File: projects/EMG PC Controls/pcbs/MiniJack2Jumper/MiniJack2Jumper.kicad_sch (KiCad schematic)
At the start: 1 part, among them J1 35RASMT2BHNTRX

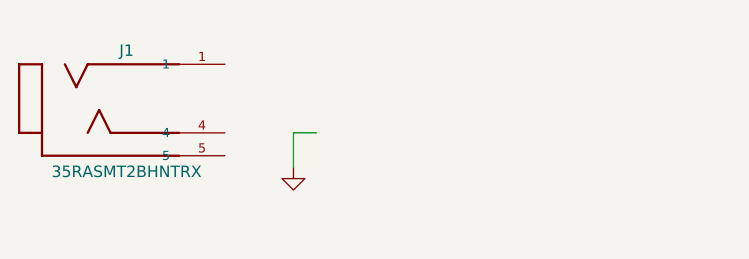
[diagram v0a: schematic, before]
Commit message: added header + BOM
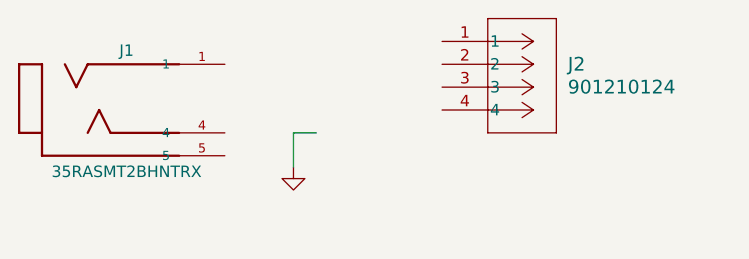
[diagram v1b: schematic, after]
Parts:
- added J2: 901210124, MiniJack2Jumper:CONN04_901210124_MOL, symbol MiniJack2Jumper:901210124
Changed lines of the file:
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@@
+	)
+	(symbol
+		(lib_id "MiniJack2Jumper:901210124")
+		(at 161.29 80.01 0)
+		(unit 1)
+		(exclude_from_sim no)
+		(in_bom yes)
+		(on_board yes)
+		(dnp no)
+		(fields_autoplaced yes)
+		(property "Reference" "J2"
+			(at 175.26 82.5499 0)
+			(effects
+				(font
+					(size 1.524 1.524)
+				)
+				(justify left)
+			)
+		)
+		(property "Value" "901210124"
+			(at 175.26 85.0899 0)
+			(effects
+				(font
+					(size 1.524 1.524)
+				)
+				(justify left)
+			)
+		)
+		(property "Footprint" "MiniJack2Jumper:CONN04_901210124_MOL"
+			(at 161.29 80.01 0)
+			(effects
+				(font
+					(size 1.27 1.27)
+					(italic yes)
+				)
+				(hide yes)
+			)
+		)
+		(property "Datasheet" "https://www.molex.com/pdm_docs/sd/901210124_sd.pdf"
+			(at 161.29 80.01 0)
+			(effects
+				(font
+					(size 1.27 1.27)
+					(italic yes)
+				)
+				(hide yes)
+			)
+		)
+		(property "Description" ""
+			(at 161.29 80.01 0)
+			(effects
+				(font
+					(size 1.27 1.27)
+				)
+				(hide yes)
+			)
+		)
+		(property "DigiKey Part Number" "23-0901210124-ND"
+			(at 161.29 80.01 0)
+			(effects
+				(font
+					(size 1.27 1.27)
+				)
+				(hide yes)
+			)
+		)
+		(property "DigiKey Link" "https://www.digikey.at/en/products/detail/molex/0901210124/760813 "
+			(at 161.29 80.01 0)
+			(effects
+				(font
+					(size 1.27 1.27)
+				)
+				(hide yes)
+			)
+		)
+		(pin "4"
+		)
+		(pin "1"
+		)
+		(pin "3"
+		)
+		(pin "2"
+		)
+		(instances
+			(project ""
+				(path "/b427ac6b-1d01-4d64-b1e2-d6e01953f973"
+					(reference "J2")
+					(unit 1)
+				)
+			)
+		)
 	)
 	(symbol

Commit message: finiished mini jack to 1x4 jumper pcb
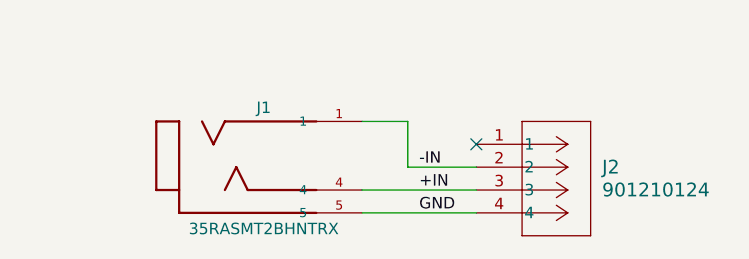
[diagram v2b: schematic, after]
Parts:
- J1: DigiKey Link (none) -> https://www.digikey.at/en/products/detail/switchcraft-inc/3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; DigiKey Part Number (none) -> SC1489-1-ND
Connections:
- net GND: now also J1.5, J2.4
- net -IN: now reaches J1.1
- net -IN: now also J2.2
- net +IN: now reaches J1.4
- net +IN: now also J2.3
- no-connect marks 0 -> 1
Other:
- moved on the sheet: J1, J2
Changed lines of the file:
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@@
 	(generator_version "8.0")
 	(paper "A4")
-	(wire
-		(pts
-			(xy 144.78 93.98) (xy 144.78 90.17)
-		)
-		(stroke
-			(width 0)
-			(type default)
-		)
-	)
-	(wire
-		(pts
-			(xy 144.78 90.17) (xy 147.32 90.17)
-		)
-		(stroke
-			(width 0)
-			(type default)
+	(no_connect
+		(at 165.1 91.44)
+	)
+	(wire
+		(pts
+			(xy 152.4 88.9) (xy 157.48 88.9)
+		)
+		(stroke
+			(width 0)
+			(type default)
+		)
+	)
+	(wire
+		(pts
+			(xy 152.4 96.52) (xy 165.1 96.52)
+		)
+		(stroke
+			(width 0)
+			(type default)
+		)
+	)
+	(wire
+		(pts
+			(xy 157.48 93.98) (xy 165.1 93.98)
+		)
+		(stroke
+			(width 0)
+			(type default)
+		)
+	)
+	(wire
+		(pts
+			(xy 157.48 88.9) (xy 157.48 93.98)
+		)
+		(stroke
+			(width 0)
+			(type default)
+		)
+	)
+	(wire
+		(pts
+			(xy 152.4 99.06) (xy 165.1 99.06)
+		)
+		(stroke
+			(width 0)
+			(type default)
+		)
+	)
+	(label "-IN"
+		(at 158.75 93.98 0)
+		(effects
+			(font
+				(size 1.27 1.27)
+			)
+			(justify left bottom)
+		)
+	)
+	(label "GND"
+		(at 158.75 99.06 0)
+		(effects
+			(font
+				(size 1.27 1.27)
+			)
+			(justify left bottom)
+		)
+	)
+	(label "+IN"
+		(at 158.75 96.52 0)
+		(effects
+			(font
+				(size 1.27 1.27)
+			)
+			(justify left bottom)
 		)
 	)
 	(symbol
 		(lib_id "MiniJack2Jumper:35RASMT2BHNTRX")
-		(at 129.54 87.63 0)
+		(at 144.78 93.98 0)
 		(unit 1)
 		(exclude_from_sim no)
@@
 		(dnp no)
 		(property "Reference" "J1"
-			(at 126.238 81.026 0)
+			(at 141.478 87.376 0)
 			(effects
 				(font
@@
 		)
 		(property "Value" "35RASMT2BHNTRX"
-			(at 126.238 94.488 0)
+			(at 141.478 100.838 0)
 			(effects
 				(font
@@
 		)
 		(property "Footprint" "MiniJack2Jumper:35RASMT2BHNTRX"
-			(at 129.54 87.63 0)
+			(at 144.78 93.98 0)
 			(effects
 				(font
@@
 			)
 		)
-		(property "Datasheet" ""
-			(at 129.54 87.63 0)
+		(property "Datasheet" "https://www.switchcraft.com/assets/1/24/35rasmt2bhntrx_cd.pdf?4698"
+			(at 144.78 93.98 0)
 			(effects
 				(font
@@
 		)
 		(property "Description" ""
-			(at 129.54 87.63 0)
+			(at 144.78 93.98 0)
 			(effects
 				(font
@@
 		)
 		(property "MANUFACTURER" "Switchcraft"
-			(at 129.54 87.63 0)
+			(at 144.78 93.98 0)
 			(effects
 				(font
@@
 				)
 				(justify bottom)
+				(hide yes)
+			)
+		)
+		(property "DigiKey Part Number" "SC1489-1-ND"
+			(at 144.78 93.98 0)
+			(effects
+				(font
+					(size 1.27 1.27)
+				)
+				(hide yes)
+			)
+		)
+		(property "DigiKey Link" "https://www.digikey.at/en/products/detail/switchcraft-inc/35RASMT2BHNTRX/1291178"
+			(at 144.78 93.98 0)
+			(effects
+				(font
+					(size 1.27 1.27)
+				)
 				(hide yes)
 			)
@@
 	(symbol
 		(lib_id "MiniJack2Jumper:901210124")
-		(at 161.29 80.01 0)
+		(at 165.1 91.44 0)
 		(unit 1)
 		(exclude_from_sim no)
@@
 		(fields_autoplaced yes)
 		(property "Reference" "J2"
-			(at 175.26 82.5499 0)
+			(at 179.07 93.9799 0)
 			(effects
 				(font
@@
 		)
 		(property "Value" "901210124"
-			(at 175.26 85.0899 0)
+			(at 179.07 96.5199 0)
 			(effects
 				(font
@@
 		)
 		(property "Footprint" "MiniJack2Jumper:CONN04_901210124_MOL"
-			(at 161.29 80.01 0)
+			(at 165.1 91.44 0)
 			(effects
 				(font
@@
 		)
 		(property "Datasheet" "https://www.molex.com/pdm_docs/sd/901210124_sd.pdf"
-			(at 161.29 80.01 0)
+			(at 165.1 91.44 0)
 			(effects
 				(font
@@
 		)
 		(property "Description" ""
-			(at 161.29 80.01 0)
+			(at 165.1 91.44 0)
 			(effects
 				(font
@@
 		)
 		(property "DigiKey Part Number" "23-0901210124-ND"
-			(at 161.29 80.01 0)
+			(at 165.1 91.44 0)
 			(effects
 				(font
@@
 		)
 		(property "DigiKey Link" "https://www.digikey.at/en/products/detail/molex/0901210124/760813 "
-			(at 161.29 80.01 0)
+			(at 165.1 91.44 0)
 			(effects
 				(font
@@
 					(unit 1)
 				)
-			)
-		)
-	)
-	(symbol
-		(lib_id "power:GND")
-		(at 144.78 93.98 0)
-		(unit 1)
-		(exclude_from_sim no)
-		(in_bom yes)
-		(on_board yes)
-		(dnp no)
-		(fields_autoplaced yes)
-		(property "Reference" "#PWR1"
-			(at 144.78 100.33 0)
-			(effects
-				(font
-					(size 1.27 1.27)
-				)
-				(hide yes)
-			)
-		)
-		(property "Value" "GND"
-			(at 144.78 99.06 0)
-			(effects
-				(font
-					(size 1.27 1.27)
-				)
-				(hide yes)
-			)
-		)
-		(property "Footprint" ""
-			(at 144.78 93.98 0)
-			(effects
-				(font
-					(size 1.27 1.27)
-				)
-				(hide yes)
-			)
-		)
-		(property "Datasheet" ""
-			(at 144.78 93.98 0)
-			(effects
-				(font
-					(size 1.27 1.27)
-				)
-				(hide yes)
-			)
-		)
-		(property "Description" "Power symbol creates a global label with name \"GND\" , ground"
-			(at 144.78 93.98 0)
-			(effects
-				(font
-					(size 1.27 1.27)
-				)
-				(hide yes)
-			)
-		)
-		(pin "1"
-		)
-		(instances
-			(project ""
-				(path "/b427ac6b-1d01-4d64-b1e2-d6e01953f973"
-					(reference "#PWR1")
-					(unit 1)
-				)
